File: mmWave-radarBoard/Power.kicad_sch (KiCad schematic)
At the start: 122 parts, among them J201 Barrel_Jack_Switch, J202 USB_C_Receptacle_USB2.0_16P, Q201 BSS123, U201 TPS628502DRLR, U202 USBLC6-2P6, U203 TPS628502DRLR, U204 TPS2116DRL, U205 XI6432BRQAAMY, U206 TLV75533PDRV

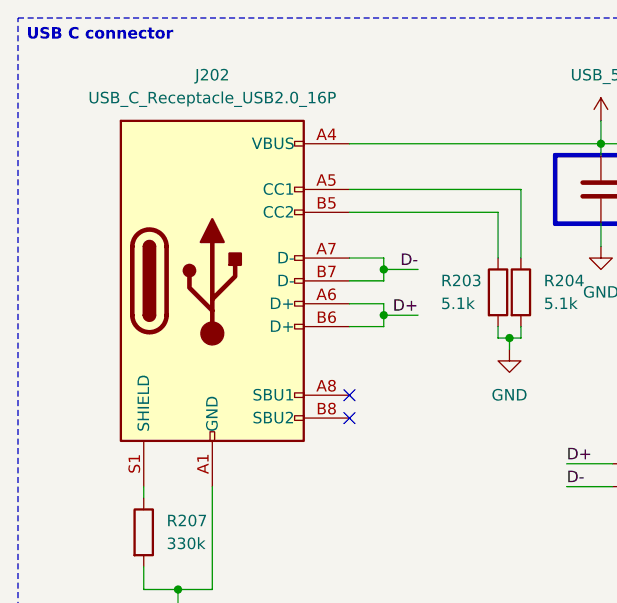
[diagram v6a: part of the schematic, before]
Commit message: Updated schematic and PCB
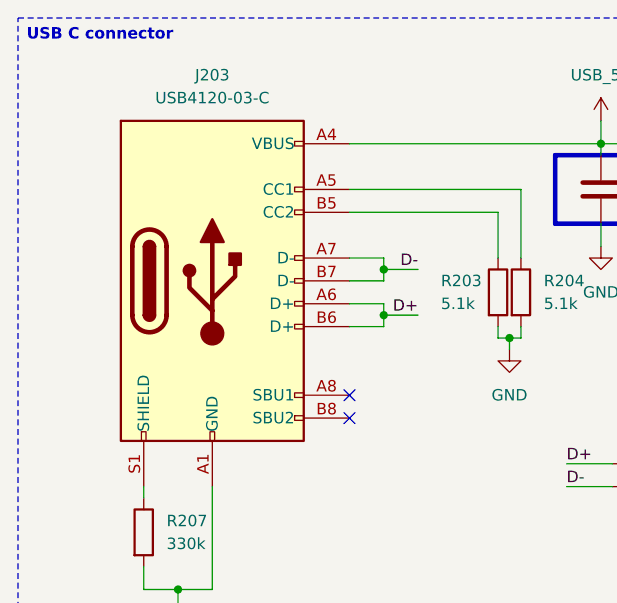
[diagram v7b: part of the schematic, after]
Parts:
- removed J202: USB_C_Receptacle_USB2.0_16P, Connector_USB:USB_C_Receptacle_G-Switch_GT-USB-7010ASV, symbol Connector:USB_C_Receptacle_USB2.0_16P
- added J203: USB4120-03-C, USB4120-03-C:GCT_USB4120-03-C, symbol USB4120-03-C:USB4120-03-C
- C235, C236, C238, C240, C241, C242, C243, C244, C247, C248, C249, C251, C252, C253, C254, C256, C259, C260, C261, C262: footprint Capacitor_SMD:C_0201_0603Metric -> Capacitor_SMD:C_0402_1005Metric
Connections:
- net D+: now also J203.A6 (D+), J203.B6 (D+)
- net D-: now also J203.A7 (D-), J203.B7 (D-)
- net GND: now also J203.A1 (GND), J203.A12 (GND), J203.B1 (GND), J203.B12 (GND)
- net USB_5V: now also J203.A4 (VBUS), J203.A9 (VBUS), J203.B4 (VBUS), J203.B9 (VBUS)
- net at R203.1: now also J203.B5 (CC2)
- net at R204.1: now also J203.A5 (CC1)
- net at R207.1: now also J203.S1 (SHIELD), J203.S2 (SHIELD), J203.S3 (SHIELD), J203.S4 (SHIELD)
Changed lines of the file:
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@@
 			)
 		)
-		(property "Footprint" "Capacitor_SMD:C_0201_0603Metric"
+		(property "Footprint" "Capacitor_SMD:C_0402_1005Metric"
 			(at 501.3452 293.37 0)
 			(effects
@@
 			)
 		)
-		(property "Footprint" "Capacitor_SMD:C_0201_0603Metric"
+		(property "Footprint" "Capacitor_SMD:C_0402_1005Metric"
 			(at 547.0652 331.47 0)
 			(effects
@@
 			)
 		)
-		(property "Footprint" "Capacitor_SMD:C_0201_0603Metric"
+		(property "Footprint" "Capacitor_SMD:C_0402_1005Metric"
 			(at 445.4652 254 0)
 			(effects
@@
 			)
 		)
-		(property "Footprint" "Capacitor_SMD:C_0201_0603Metric"
+		(property "Footprint" "Capacitor_SMD:C_0402_1005Metric"
 			(at 441.6552 293.37 0)
 			(effects
@@
 			)
 		)
-		(property "Footprint" "Capacitor_SMD:C_0201_0603Metric"
+		(property "Footprint" "Capacitor_SMD:C_0402_1005Metric"
 			(at 482.2952 254 0)
 			(effects
@@
 			)
 		)
-		(property "Footprint" "Capacitor_SMD:C_0201_0603Metric"
+		(property "Footprint" "Capacitor_SMD:C_0402_1005Metric"
 			(at 455.6252 331.47 0)
 			(effects
@@
 			)
 		)
-		(property "Footprint" "Capacitor_SMD:C_0201_0603Metric"
+		(property "Footprint" "Capacitor_SMD:C_0402_1005Metric"
 			(at 486.1052 293.37 0)
 			(effects
@@
 			)
 		)
-		(property "Footprint" "Capacitor_SMD:C_0201_0603Metric"
+		(property "Footprint" "Capacitor_SMD:C_0402_1005Metric"
 			(at 517.8552 331.47 0)
 			(effects
@@
 			)
 		)
-		(property "Footprint" "Capacitor_SMD:C_0201_0603Metric"
+		(property "Footprint" "Capacitor_SMD:C_0402_1005Metric"
 			(at 525.4752 254 0)
 			(effects
@@
 			)
 		)
-		(property "Footprint" "Capacitor_SMD:C_0201_0603Metric"
+		(property "Footprint" "Capacitor_SMD:C_0402_1005Metric"
 			(at 554.6852 254 0)
 			(effects
@@
 			)
 		)
-		(property "Footprint" "Capacitor_SMD:C_0201_0603Metric"
+		(property "Footprint" "Capacitor_SMD:C_0402_1005Metric"
 			(at 390.8552 331.47 0)
 			(effects
@@
 			)
 		)
-		(property "Footprint" "Capacitor_SMD:C_0201_0603Metric"
+		(property "Footprint" "Capacitor_SMD:C_0402_1005Metric"
 			(at 502.6152 331.47 0)
 			(effects
@@
 	)
 	(symbol
-		(lib_id "Connector:USB_C_Receptacle_USB2.0_16P")
-		(at 54.61 86.36 0)
-		(unit 1)
-		(exclude_from_sim no)
-		(in_bom yes)
-		(on_board yes)
-		(dnp no)
-		(fields_autoplaced yes)
-		(property "Reference" "J202"
-			(at 54.61 63.5 0)
-			(effects
-				(font
-					(size 1.27 1.27)
-				)
-			)
-		)
-		(property "Value" "USB_C_Receptacle_USB2.0_16P"
-			(at 54.61 66.04 0)
-			(effects
-				(font
-					(size 1.27 1.27)
-				)
-			)
-		)
-		(property "Footprint" "Connector_USB:USB_C_Receptacle_G-Switch_GT-USB-7010ASV"
-			(at 58.42 86.36 0)
-			(effects
-				(font
-					(size 1.27 1.27)
-				)
-				(hide yes)
-			)
-		)
-		(property "Datasheet" "https://www.usb.org/sites/default/files/documents/usb_type-c.zip"
-			(at 58.42 86.36 0)
-			(effects
-				(font
-					(size 1.27 1.27)
-				)
-				(hide yes)
-			)
-		)
-		(property "Description" "USB 2.0-only 16P Type-C Receptacle connector"
-			(at 54.61 86.36 0)
-			(effects
-				(font
-					(size 1.27 1.27)
-				)
-				(hide yes)
-			)
-		)
-		(pin "A12"
-		)
-		(pin "B1"
-		)
-		(pin "B6"
-		)
-		(pin "A1"
-		)
-		(pin "A4"
-		)
-		(pin "A9"
-		)
-		(pin "B4"
-		)
-		(pin "B9"
-		)
-		(pin "A7"
-		)
-		(pin "B7"
-		)
-		(pin "A6"
-		)
-		(pin "A8"
-		)
-		(pin "B8"
-		)
-		(pin "B12"
-		)
-		(pin "B5"
-		)
-		(pin "S1"
-		)
-		(pin "A5"
-		)
-		(instances
-			(project ""
-				(path "/65d1bf45-0c7d-403c-8da5-e1777d98e937/63e9aa23-19c0-43a2-8100-8d16d5100cb9"
-					(reference "J202")
-					(unit 1)
-				)
-			)
-		)
-	)
-	(symbol
 		(lib_id "power:GND")
 		(at 261.62 207.01 0)
@@
 			)
 		)
-		(property "Footprint" "Capacitor_SMD:C_0201_0603Metric"
+		(property "Footprint" "Capacitor_SMD:C_0402_1005Metric"
 			(at 406.0952 254 0)
 			(effects
@@
 	)
 	(symbol
+		(lib_id "USB4120-03-C:USB4120-03-C")
+		(at 54.61 86.36 0)
+		(unit 1)
+		(exclude_from_sim no)
+		(in_bom yes)
+		(on_board yes)
+		(dnp no)
+		(fields_autoplaced yes)
+		(property "Reference" "J203"
+			(at 54.61 63.5 0)
+			(effects
+				(font
+					(size 1.27 1.27)
+				)
+			)
+		)
+		(property "Value" "USB4120-03-C"
+			(at 54.61 66.04 0)
+			(effects
+				(font
+					(size 1.27 1.27)
+				)
+			)
+		)
+		(property "Footprint" "USB4120-03-C:GCT_USB4120-03-C"
+			(at 54.61 118.11 0)
+			(effects
+				(font
+					(size 1.27 1.27)
+				)
+				(justify bottom)
+				(hide yes)
+			)
+		)
+		(property "Datasheet" ""
+			(at 54.61 86.36 0)
+			(effects
+				(font
+					(size 1.27 1.27)
+				)
+				(hide yes)
+			)
+		)
+		(property "Description" ""
+			(at 54.61 86.36 0)
+			(effects
+				(font
+					(size 1.27 1.27)
+				)
+				(hide yes)
+			)
+		)
+		(property "MF" "Global Connector Technology"
+			(at 54.61 118.11 0)
+			(effects
+				(font
+					(size 1.27 1.27)
+				)
+				(justify bottom)
+				(hide yes)
+			)
+		)
+		(property "MAXIMUM_PACKAGE_HEIGHT" "6.5mm"
+			(at 54.61 118.11 0)
+			(effects
+				(font
+					(size 1.27 1.27)
+				)
+				(justify bottom)
+				(hide yes)
+			)
+		)
+		(property "Package" "None"
+			(at 54.61 118.11 0)
+			(effects
+				(font
+					(size 1.27 1.27)
+				)
+				(justify bottom)
+				(hide yes)
+			)
+		)
+		(property "Price" "None"
+			(at 54.61 118.11 0)
+			(effects
+				(font
+					(size 1.27 1.27)
+				)
+				(justify bottom)
+				(hide yes)
+			)
+		)
+		(property "Check_prices" "https://www.snapeda.com/parts/USB4120-03-C/Global+Connector+Technology/view-part/?ref=eda"
+			(at 54.61 118.11 0)
+			(effects
+				(font
+					(size 1.27 1.27)
+				)
+				(justify bottom)
+				(hide yes)
+			)
+		)
+		(property "STANDARD" "Manufacturer Recommendations"
+			(at 54.61 118.11 0)
+			(effects
+				(font
+					(size 1.27 1.27)
+				)
+				(justify bottom)
+				(hide yes)
+			)
+		)
+		(property "PARTREV" "A"
+			(at 54.61 118.11 0)
+			(effects
+				(font
+					(size 1.27 1.27)
+				)
+				(justify bottom)
+				(hide yes)
+			)
+		)
+		(property "SnapEDA_Link" "https://www.snapeda.com/parts/USB4120-03-C/Global+Connector+Technology/view-part/?ref=snap"
+			(at 54.61 118.11 0)
+			(effects
+				(font
+					(size 1.27 1.27)
+				)
+				(justify bottom)
+				(hide yes)
+			)
+		)
+		(property "MP" "USB4120-03-C"
+			(at 54.61 118.11 0)
+			(effects
+				(font
+					(size 1.27 1.27)
+				)
+				(justify bottom)
+				(hide yes)
+			)
+		)
+		(property "Description_1" "USB 2.0 Connector Type C Vertical Receptacle, 6.50mm profile, 16 Pins, Surface mount, Top mount, low profile, low cost"
+			(at 54.61 118.11 0)
+			(effects
+				(font
+					(size 1.27 1.27)
+				)
+				(justify bottom)
+				(hide yes)
+			)
+		)
+		(property "Availability" "In Stock"
+			(at 54.61 118.11 0)
+			(effects
+				(font
+					(size 1.27 1.27)
+				)
+				(justify bottom)
+				(hide yes)
+			)
+		)
+		(property "MANUFACTURER" "GCT"
+			(at 54.61 118.11 0)
+			(effects
+				(font
+					(size 1.27 1.27)
+				)
+				(justify bottom)
+				(hide yes)
+			)
+		)
+		(pin "S3"
+		)
+		(pin "A12"
+		)
+		(pin "B12"
+		)
+		(pin "B4"
+		)
+		(pin "A4"
+		)
+		(pin "S2"
+		)
+		(pin "S1"
+		)
+		(pin "S4"
+		)
+		(pin "A1"
+		)
+		(pin "B1"
+		)
+		(pin "A9"
+		)
+		(pin "B9"
+		)
+		(pin "A5"
+		)
+		(pin "B5"
+		)
+		(pin "A7"
+		)
+		(pin "B7"
+		)
+		(pin "A6"
+		)
+		(pin "A8"
+		)
+		(pin "B6"
+		)
+		(pin "B8"
+		)
+		(instances
+			(project ""
+				(path "/65d1bf45-0c7d-403c-8da5-e1777d98e937/63e9aa23-19c0-43a2-8100-8d16d5100cb9"
+					(reference "J203")
+					(unit 1)
+				)
+			)
+		)
+	)
+	(symbol
 		(lib_id "Device:C")
 		(at 504.19 250.19 0)
@@
 			)
 		)
-		(property "Footprint" "Capacitor_SMD:C_0201_0603Metric"
+		(property "Footprint" "Capacitor_SMD:C_0402_1005Metric"
 			(at 505.1552 254 0)
 			(effects
@@
 			)
 		)
-		(property "Footprint" "Capacitor_SMD:C_0201_0603Metric"
+		(property "Footprint" "Capacitor_SMD:C_0402_1005Metric"
 			(at 390.8552 293.37 0)
 			(effects
@@
 			)
 		)
-		(property "Footprint" "Capacitor_SMD:C_0201_0603Metric"
+		(property "Footprint" "Capacitor_SMD:C_0402_1005Metric"
 			(at 390.8552 254 0)
 			(effects
@@
 			)
 		)
-		(property "Footprint" "Capacitor_SMD:C_0201_0603Metric"
+		(property "Footprint" "Capacitor_SMD:C_0402_1005Metric"
 			(at 414.9852 293.37 0)
 			(effects
@@
 			)
 		)
-		(property "Footprint" "Capacitor_SMD:C_0201_0603Metric"
+		(property "Footprint" "Capacitor_SMD:C_0402_1005Metric"
 			(at 533.0952 331.47 0)
 			(effects
@@
 			)
 		)
-		(property "Footprint" "Capacitor_SMD:C_0201_0603Metric"
+		(property "Footprint" "Capacitor_SMD:C_0402_1005Metric"
 			(at 539.4452 254 0)
 			(effects
@@
 			)
 		)
-		(property "Footprint" "Capacitor_SMD:C_0201_0603Metric"
+		(property "Footprint" "Capacitor_SMD:C_0402_1005Metric"
 			(at 414.9852 331.47 0)
 			(effects

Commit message: Updated PCB and schematic
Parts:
- removed J201: Barrel_Jack_Switch, Connector_BarrelJack:BarrelJack_GCT_DCJ200-10-A_Horizontal, symbol Connector:Barrel_Jack_Switch
- added J201: Conn_01x02_Socket, Connector_JST:JST_ZH_B2B-ZR_1x02_P1.50mm_Vertical, symbol Connector:Conn_01x02_Socket
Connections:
- net GND: now also J201.2 (Pin_2)
- net at F201.1: now also J201.1 (Pin_1)
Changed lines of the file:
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@@
 	(text "5V 3A"
 		(exclude_from_sim no)
-		(at 222.25 90.17 0)
+		(at 228.6 86.36 0)
 		(effects
 			(font
@@
 	)
 	(junction
-		(at 232.41 85.09)
-		(diameter 0)
-		(color 0 0 0 0)
-	)
-	(junction
 		(at 189.23 81.28)
 		(diameter 0)
@@
 	(wire
 		(pts
-			(xy 229.87 80.01) (xy 236.22 80.01)
+			(xy 231.14 80.01) (xy 236.22 80.01)
 		)
 		(stroke
@@
 	(wire
 		(pts
-			(xy 229.87 82.55) (xy 232.41 82.55)
+			(xy 231.14 82.55) (xy 233.68 82.55)
 		)
 		(stroke
@@
 	(wire
 		(pts
-			(xy 232.41 85.09) (xy 232.41 92.71)
+			(xy 233.68 82.55) (xy 233.68 92.71)
 		)
 		(stroke
@@
 	(wire
 		(pts
-			(xy 229.87 85.09) (xy 232.41 85.09)
-		)
-		(stroke
-			(width 0)
-			(type default)
-		)
-	)
-	(wire
-		(pts
 			(xy 149.86 262.89) (xy 151.13 262.89)
 		)
@@
 	(wire
 		(pts
-			(xy 232.41 82.55) (xy 232.41 85.09)
-		)
-		(stroke
-			(width 0)
-			(type default)
-		)
-	)
-	(wire
-		(pts
 			(xy 485.14 294.64) (xy 500.38 294.64)
 		)
@@
 	)
 	(symbol
-		(lib_id "Connector:Barrel_Jack_Switch")
-		(at 222.25 82.55 0)
-		(unit 1)
-		(exclude_from_sim no)
-		(in_bom yes)
-		(on_board yes)
-		(dnp no)
-		(fields_autoplaced yes)
-		(property "Reference" "J201"
-			(at 222.25 73.66 0)
-			(effects
-				(font
-					(size 1.27 1.27)
-				)
-			)
-		)
-		(property "Value" "Barrel_Jack_Switch"
-			(at 222.25 76.2 0)
-			(effects
-				(font
-					(size 1.27 1.27)
-				)
-			)
-		)
-		(property "Footprint" "Connector_BarrelJack:BarrelJack_GCT_DCJ200-10-A_Horizontal"
-			(at 223.52 83.566 0)
-			(effects
-				(font
-					(size 1.27 1.27)
-				)
-				(hide yes)
-			)
-		)
-		(property "Datasheet" "~"
-			(at 223.52 83.566 0)
-			(effects
-				(font
-					(size 1.27 1.27)
-				)
-				(hide yes)
-			)
-		)
-		(property "Description" "DC Barrel Jack with an internal switch"
-			(at 222.25 82.55 0)
-			(effects
-				(font
-					(size 1.27 1.27)
-				)
-				(hide yes)
-			)
-		)
-		(pin "1"
-		)
-		(pin "3"
-		)
-		(pin "2"
-		)
-		(instances
-			(project ""
-				(path "/65d1bf45-0c7d-403c-8da5-e1777d98e937/63e9aa23-19c0-43a2-8100-8d16d5100cb9"
-					(reference "J201")
-					(unit 1)
-				)
-			)
-		)
-	)
-	(symbol
 		(lib_id "power:GND")
 		(at 97.79 82.55 0)
@@
 	(symbol
 		(lib_id "power:GND")
-		(at 232.41 92.71 0)
+		(at 233.68 92.71 0)
 		(unit 1)
 		(exclude_from_sim no)
@@
 		(fields_autoplaced yes)
 		(property "Reference" "#PWR0214"
-			(at 232.41 99.06 0)
+			(at 233.68 99.06 0)
 			(effects
 				(font
@@
 		)
 		(property "Value" "GND"
-			(at 232.41 97.79 0)
+			(at 233.68 97.79 0)
 			(effects
 				(font
@@
 		)
 		(property "Footprint" ""
-			(at 232.41 92.71 0)
+			(at 233.68 92.71 0)
 			(effects
 				(font
@@
 		)
 		(property "Datasheet" ""
-			(at 232.41 92.71 0)
+			(at 233.68 92.71 0)
 			(effects
 				(font
@@
 		)
 		(property "Description" "Power symbol creates a global label with name \"GND\" , ground"
-			(at 232.41 92.71 0)
+			(at 233.68 92.71 0)
 			(effects
 				(font
@@
 					(unit 1)
 				)
+			)
+		)
+	)
+	(symbol
+		(lib_id "Connector:Conn_01x02_Socket")
+		(at 226.06 80.01 0)
+		(mirror y)
+		(unit 1)
+		(exclude_from_sim no)
+		(in_bom yes)
+		(on_board yes)
+		(dnp no)
+		(fields_autoplaced yes)
+		(property "Reference" "J201"
+			(at 226.695 74.93 0)
+			(effects
+				(font
+					(size 1.27 1.27)
+				)
+			)
+		)
+		(property "Value" "Conn_01x02_Socket"
+			(at 226.695 77.47 0)
+			(effects
+				(font
+					(size 1.27 1.27)
+				)
+			)
+		)
+		(property "Footprint" "Connector_JST:JST_ZH_B2B-ZR_1x02_P1.50mm_Vertical"
+			(at 226.06 80.01 0)
+			(effects
+				(font
+					(size 1.27 1.27)
+				)
+				(hide yes)
+			)
+		)
+		(property "Datasheet" "~"
+			(at 226.06 80.01 0)
+			(effects
+				(font
+					(size 1.27 1.27)
+				)
+				(hide yes)
+			)
+		)
+		(property "Description" "Generic connector, single row, 01x02, script generated"
+			(at 226.06 80.01 0)
+			(effects
+				(font
+					(size 1.27 1.27)
+				)
+				(hide yes)
+			)
+		)
+		(pin "1"
+		)
+		(pin "2"
+		)
+		(instances
+			(project ""
+				(path "/65d1bf45-0c7d-403c-8da5-e1777d98e937/63e9aa23-19c0-43a2-8100-8d16d5100cb9"
+					(reference "J201")
+					(unit 1)
+				)
